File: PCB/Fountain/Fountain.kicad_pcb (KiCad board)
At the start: 2 copper layers, 100 x 86.6 mm, 29 parts, among them CN1 GROVE_IIC_5V, CN2 GROVE_IIC_5V, CN3 USB_A, CN4 AudioJack3_SwitchTR, CN5 Micro_SD_Card_Det_Hirose_DM3AT, J1 Speaker, SW1 MDOE, SW2 NEXT/VOL+, SW3 PREV/VOL-, U1 SeeeduinoXIAO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

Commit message: (Fountain) 基板位置仮決め #77
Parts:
- removed C1, C2: 100u, Capacitor_THT:CP_Radial_D6.3mm_P2.50mm
- removed CN5: Micro_SD_Card_Det_Hirose_DM3AT, Connector_Card:microSD_HC_Hirose_DM3AT-SF-PEJM5
- removed J1: Speaker, Connector_PinHeader_2.54mm:PinHeader_1x02_P2.54mm_Vertical
- removed R3, R4, R5: 4.7k, Resistor_THT:R_Axial_DIN0207_L6.3mm_D2.5mm_P7.62mm_Horizontal
- removed R6, R7: 1k, Resistor_THT:R_Axial_DIN0207_L6.3mm_D2.5mm_P7.62mm_Horizontal
- removed RV1: BRIGHTNESS, Potentiometer_THT:Potentiometer_Alps_RK097_Dual_Horizontal
- removed RV2: VOLUME, Potentiometer_THT:Potentiometer_Alps_RK097_Dual_Horizontal
- removed U1: SeeeduinoXIAO, extsui:SeeeduinoXIAO
- removed U2: DFPlayerMini, extsui:DFPlayerMini
- removed U3: OLED_128x64_IIC, extsui:OLED_128x64_0.96inch
- added BZ1: Buzzer, Buzzer_Beeper:Buzzer_TDK_PS1240P02BT_D12.2mm_H6.5mm, F.Cu at (152.5, 105.2)
- added IC1: XIAO-ESP32-C3, extsui:SeeeduinoXIAO, F.Cu at (130.0, 62.0)
- added IC2: AE-PCA9306, Package_DIP:DIP-8_W7.62mm_Socket, F.Cu at (142.5, 84.8)
- added VOL1: (TBD), Potentiometer_THT:Potentiometer_Alps_RK097_Dual_Horizontal, F.Cu at (115.5, 143.0)
- added VOL2: (TBD), Potentiometer_THT:Potentiometer_Alps_RK097_Dual_Horizontal, F.Cu at (139.5, 143.0)
- CN1: value GROVE_IIC_5V -> Conn_01x05_Female; footprint Connector:NS-Tech_Grove_1x04_P2mm_Vertical -> Connector_PinHeader_2.54mm:PinHeader_1x05_P2.54mm_Vertical
- CN2: value GROVE_IIC_5V -> CardEdgeConnector5P; footprint Connector:NS-Tech_Grove_1x04_P2mm_Vertical -> extsui:CONN_CARD_EDGE_395-010-521-201
- CN3: value USB_A -> GROVE_IIC_5V; footprint OPL_Connector:USB4+2P-2.0-90D -> OPL_Connector:HW4-2.0-90D
- CN4: value AudioJack3_SwitchTR -> GROVE_IIC_5V; footprint Connector_Audio:Jack_3.5mm_Ledino_KB3SPRS_Horizontal -> OPL_Connector:HW4-2.0-90D
- R1: value 4.7k -> 10k
- R2: value 4.7k -> 1k
- SW1: value MDOE -> (TBD)
- SW2: value NEXT/VOL+ -> (TBD)
- SW3: value PREV/VOL- -> DIPSW-4P; footprint Button_Switch_THT:SW_PUSH_6mm_H8.5mm -> Button_Switch_THT:SW_DIP_SPSTx04_Slide_9.78x12.34mm_W7.62mm_P2.54mm
- moved SW3 52.5 mm to (101.8, 108.5), turned to 90 degrees
- moved CN2 38.5 mm to (130.0, 105.0)
- moved SW1 35.5 mm to (97.8, 121.5), turned to 300 degrees
- moved CN4 30.6 mm to (161.8, 85.8), turned to 300 degrees
- moved CN1 25.0 mm to (125.2, 92.8), turned to 90 degrees
- moved R1 14.7 mm to (145.5, 77.2), turned to 90 degrees
- moved R2 14.4 mm to (145.0, 98.2), turned to 0 degrees
- moved SW2 9.04 mm to (160.5, 124.8)
- moved CN3 4.31 mm to (98.0, 85.8), turned to 60 degrees
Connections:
- CN1 pad 1: SCL -> 5V
- CN1 pad 2: SDA -> SDA_5V
- CN1 pad 3: 5V -> SCL_5V
- CN1 pad 4: GND -> Net-(CN1-Pad4)
- CN2 pad 1: SCL -> 5V
- CN2 pad 2: SDA -> SDA_5V
- CN2 pad 3: 5V -> SCL_5V
- CN2 pad 4: GND -> Net-(CN2-Pad4)
- CN3 pad 1: 5V -> SCL_5V
- CN3 pad 2: Net-(CN3-Pad2) -> SDA_5V
- CN3 pad 3: Net-(CN3-Pad3) -> 5V
- R1 pad 1: 3V3 -> Net-(IC1-Pad9)
- R1 pad 2: SDA -> 3V3
- R2 pad 1: 3V3 -> Net-(IC1-Pad7)
- R2 pad 2: SCL -> Net-(BZ1-Pad1)
- SW1 pad 1: Net-(SW1-Pad1) -> Net-(IC1-Pad9)
- SW3 pad 1: Net-(SW3-Pad1) -> GND
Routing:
- net 3V3: track 185.6 -> 0.00 mm
- net GND: track 131.3 -> 0.00 mm, vias 283 -> 58
- net 5V: track 110.0 -> 0.00 mm
- net RV_V: track 96.9 -> 0.00 mm, vias 2 -> 0
- net Net-(SW1-Pad1): track 87.7 -> 0.00 mm, vias 2 -> 0
- net MOSI: track 82.9 -> 0.00 mm
- net MISO: track 82.8 -> 0.00 mm, vias 1 -> 0
- net SCK: track 78.6 -> 0.00 mm, vias 1 -> 0
- net SCL: track 75.0 -> 0.00 mm, vias 1 -> 0
- net SDA: track 71.7 -> 0.00 mm, vias 1 -> 0
- net RV_B: track 70.2 -> 0.00 mm, vias 2 -> 0
- net Net-(IC1-Pad10): track 66.8 -> 0.00 mm
- net CS: track 60.6 -> 0.00 mm, vias 1 -> 0
- net Net-(SW3-Pad1): track 58.6 -> 0.00 mm
- net TXD: track 52.2 -> 0.00 mm, vias 1 -> 0
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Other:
- board text added: "@ext_sui 2023.10"
- board text added: "Fountain v1.0"
- board text removed: "@ext_sui 2021.09"
- board text removed: "BRIGHTNESS"
- board text removed: "C"
- board text removed: "D"
- board text removed: "G"
- board text removed: "MODE"
- board text removed: "NEXT+"
- board text removed: "PREV-"
- board text removed: "SPK"
- board text removed: "Ship Growing v1.0"
- board text removed: "V"
- board text removed: "VOLUME"

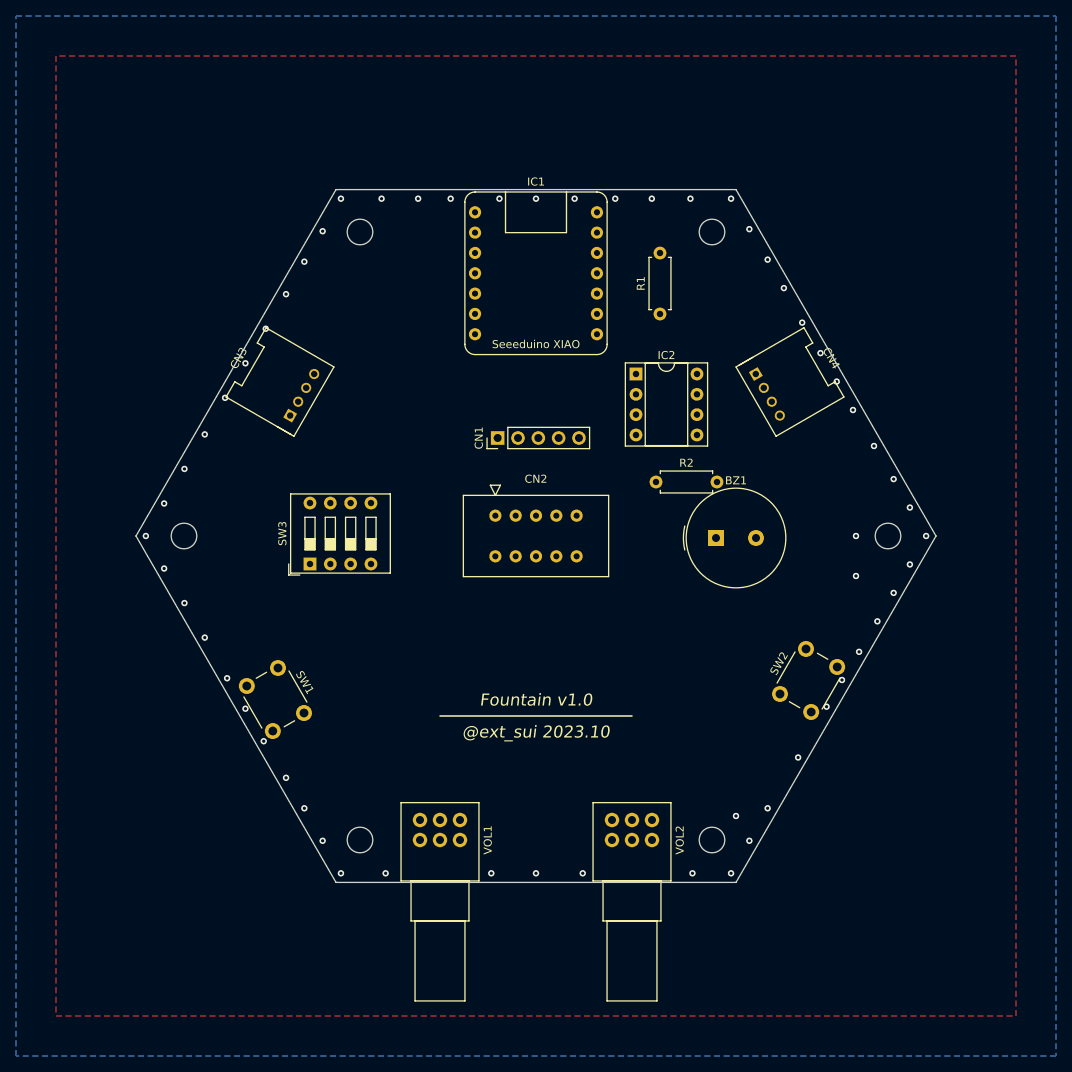
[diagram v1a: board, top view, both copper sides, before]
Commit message: (Fountain) JTAG コネクタと電解コンを追加および VOL/SW 位置調整 #77
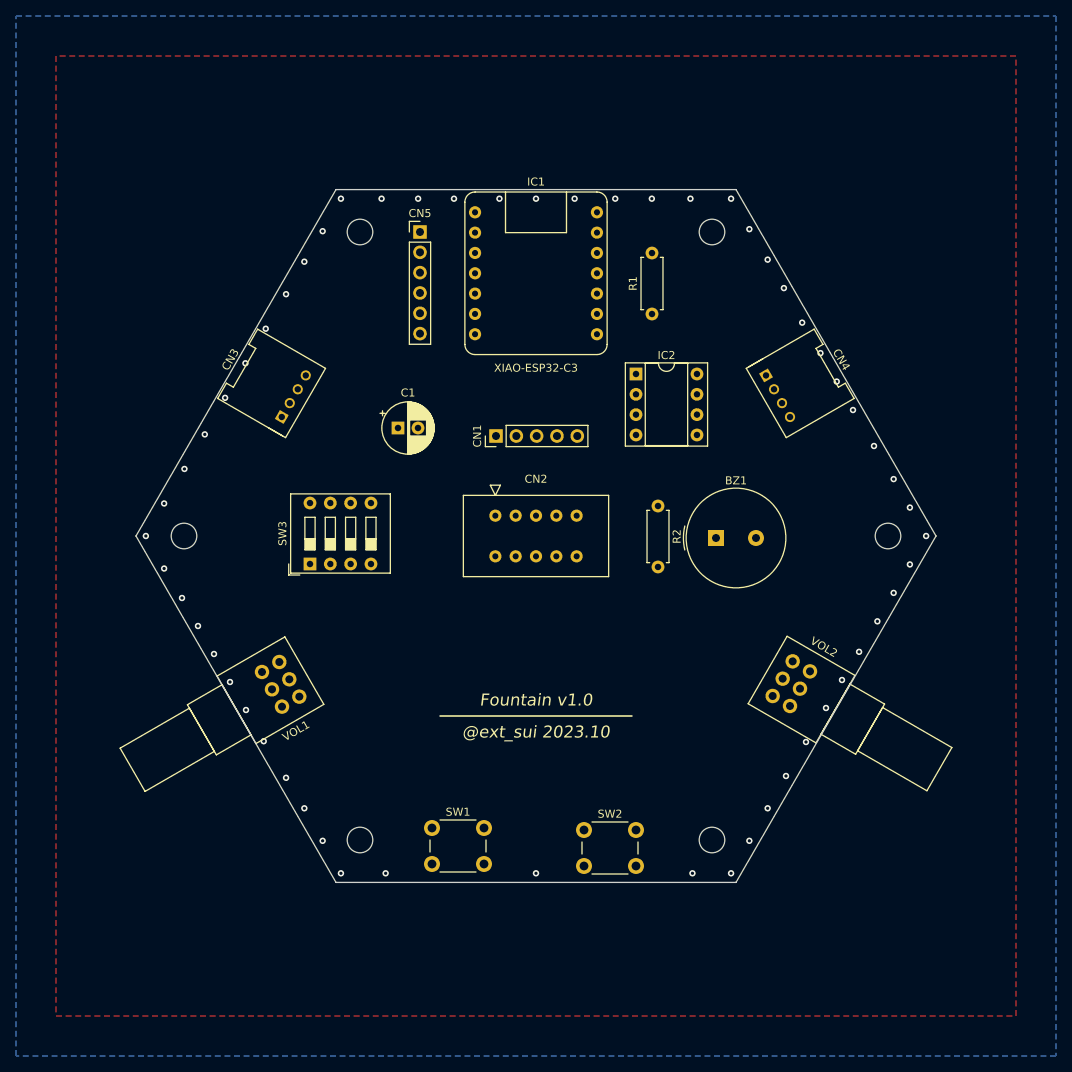
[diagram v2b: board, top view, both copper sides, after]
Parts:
- added C1: CP, Capacitor_THT:CP_Radial_D6.3mm_P2.50mm, F.Cu at (112.8, 91.5)
- added CN5: JTAG, Connector_PinHeader_2.54mm:PinHeader_1x06_P2.54mm_Vertical, F.Cu at (115.5, 67.0)
- moved SW2 29.8 mm to (136.0, 141.8), turned to 0 degrees
- moved VOL1 28.8 mm to (95.8, 122.0), turned to 210 degrees
- moved VOL2 27.9 mm to (161.8, 126.2), turned to 330 degrees
- moved SW1 27.8 mm to (117.0, 141.5), turned to 0 degrees
- moved R2 3.01 mm to (145.2, 101.2), turned to 270 degrees
- moved CN4 1.29 mm to (163.0, 85.9)
- moved CN3 1.06 mm to (97.0, 85.9)
- moved R1 1.00 mm to (144.5, 77.2)
- moved CN1 0.33 mm to (125.0, 92.5)
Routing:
- net GND: vias 58 -> 55

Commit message: (Fountain) 部品位置仮決めとシルク追加 #77
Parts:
- moved BZ1 1.00 mm to (153.5, 105.2)
- moved SW1 1.00 mm to (118.0, 141.5)
- moved SW2 0.56 mm to (135.5, 141.5)
- moved SW3 0.31 mm to (101.8, 108.8)
- moved R2 0.25 mm to (145.5, 101.2)
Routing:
- net GND: vias 55 -> 59
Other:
- board text added: "+5V"
- board text added: "GND"
- board text added: "TCK"
- board text added: "TDI"
- board text added: "TDO"
- board text added: "TMS"

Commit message: (Fountain) 配線試行 #77
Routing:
- net 5V: track 0.00 -> 154.5 mm
- net SCL_5V: track 0.00 -> 115.6 mm
- net RV2: track 0.00 -> 97.9 mm
- net SDA_5V: track 0.00 -> 94.6 mm
- net RV1: track 0.00 -> 80.2 mm
- net Net-(CN5-Pad3): track 0.00 -> 45.9 mm
- net Net-(IC1-Pad7): track 0.00 -> 42.3 mm, vias 0 -> 1
- net Net-(CN5-Pad4): track 0.00 -> 42.0 mm
- net Net-(CN5-Pad5): track 0.00 -> 38.4 mm
- net Net-(CN5-Pad6): track 0.00 -> 34.5 mm
- net SDA_3V3: track 0.00 -> 22.6 mm
- net 3V3: track 0.00 -> 22.5 mm
- net GND: track 0.00 -> 15.1 mm
- net SCL_3V3: track 0.00 -> 10.9 mm
- net Net-(BZ1-Pad1): track 0.00 -> 9.50 mm
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
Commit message: (Fountain) 配線第0版完成 #77
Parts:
- moved BZ1 3.59 mm to (156.0, 107.8), turned to 90 degrees
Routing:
- net 3V3: track 22.5 -> 136.4 mm, vias 0 -> 3
- net Net-(IC1-Pad9): track 6.88 -> 87.2 mm, vias 0 -> 1
- net Net-(IC1-Pad10): track 0.00 -> 76.9 mm, vias 0 -> 1
- net SDA_5V: track 94.6 -> 111.6 mm, vias 1 -> 0
- net GND: track 15.1 -> 0.11 mm, vias 59 -> 61
- net RV1: track 80.2 -> 84.2 mm, vias 0 -> 2
- net RV2: track 97.9 -> 94.9 mm, vias 0 -> 2
- net Net-(IC1-Pad7): track 42.3 -> 40.0 mm
- net Net-(CN5-Pad3): track 45.9 -> 47.7 mm
- net Net-(BZ1-Pad1): track 9.50 -> 11.0 mm
- net Net-(CN5-Pad4): track 42.0 -> 43.4 mm
- net SCL_5V: track 115.6 -> 114.5 mm
- net Net-(CN5-Pad5): track 38.4 -> 38.9 mm
- net Net-(VOL1-Pad1): vias 1 -> 0

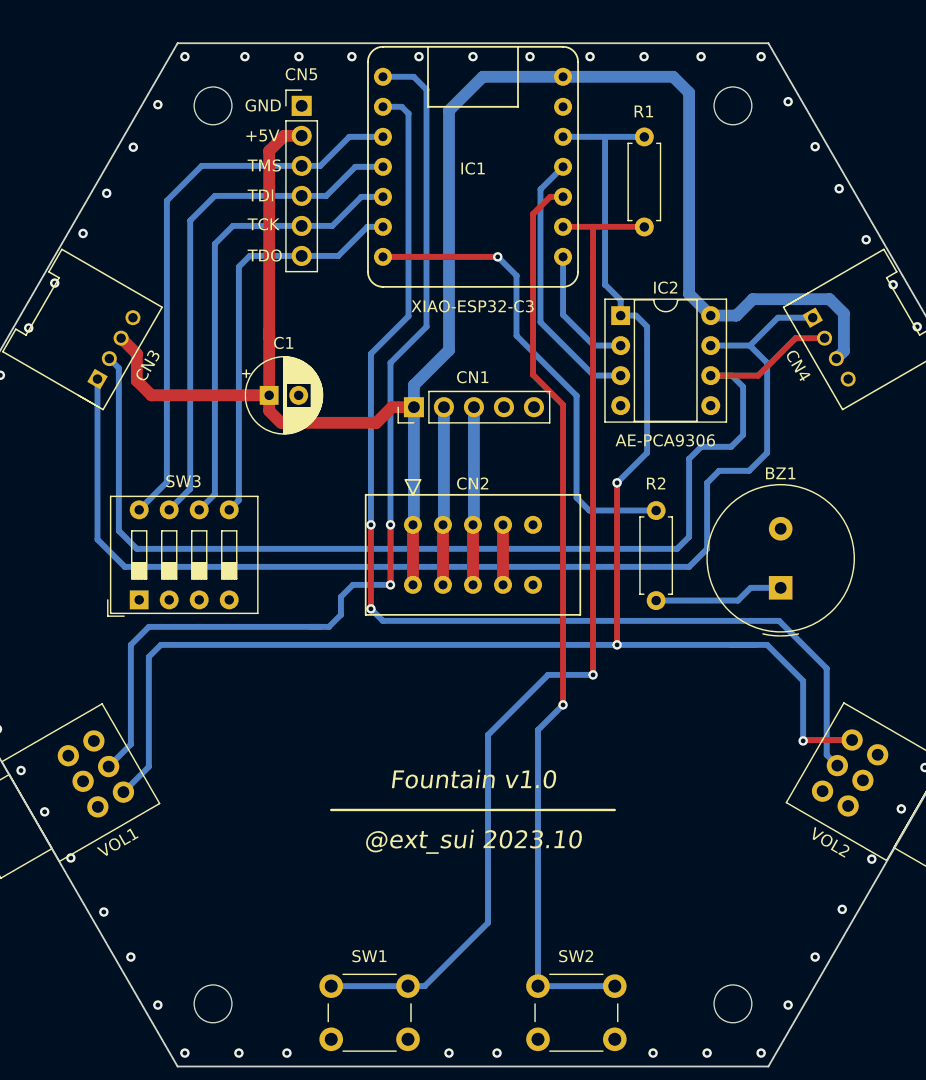
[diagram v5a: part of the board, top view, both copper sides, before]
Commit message: (Fountain) 配線調整とシルク修正 #77
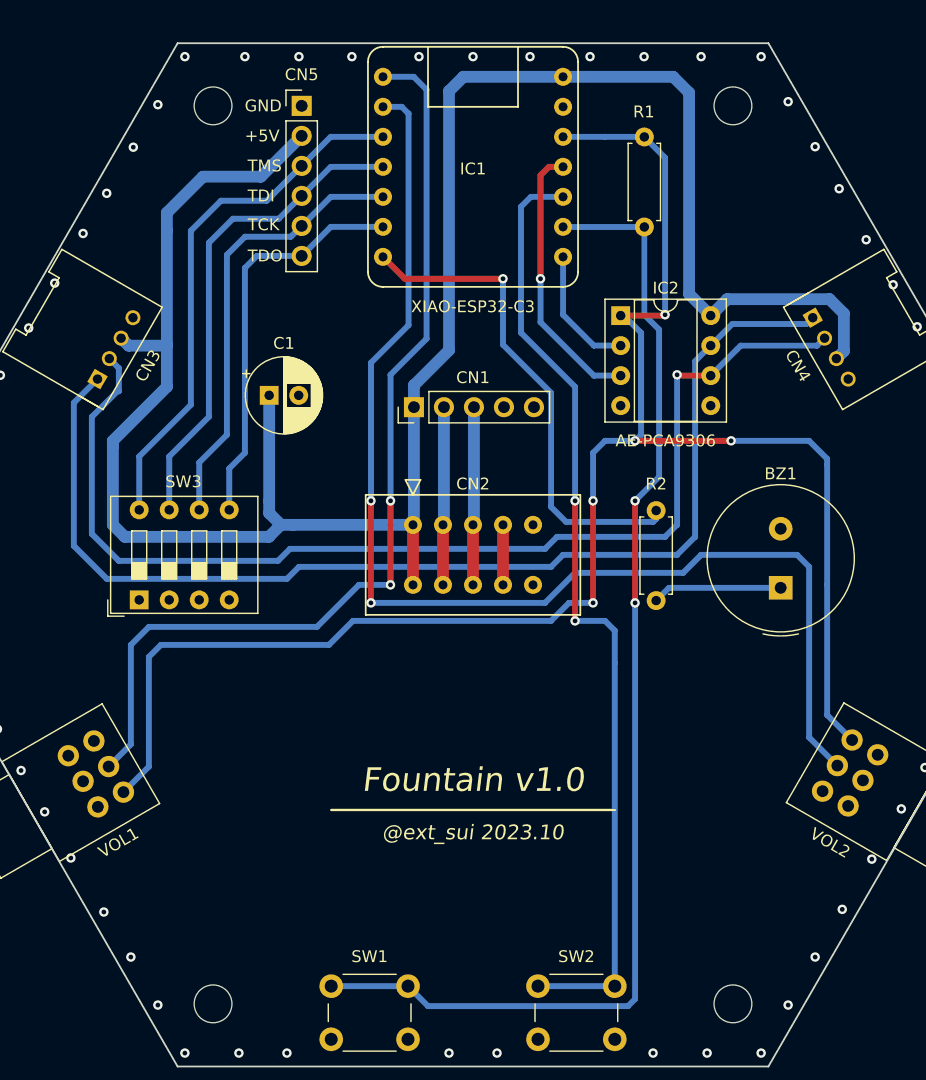
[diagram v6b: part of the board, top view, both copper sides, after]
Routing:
- net 5V: track 154.4 -> 184.7 mm
- net 3V3: track 136.4 -> 155.8 mm, vias 3 -> 5
- net Net-(IC1-Pad9): track 87.2 -> 100.3 mm, vias 1 -> 2
- net RV2: track 94.9 -> 102.1 mm
- net Net-(IC1-Pad10): track 76.9 -> 81.1 mm, vias 1 -> 2
- net Net-(CN5-Pad3): track 47.7 -> 45.0 mm
- net Net-(IC1-Pad7): track 40.0 -> 42.1 mm
- net Net-(CN5-Pad4): track 43.4 -> 41.4 mm
- net RV1: track 84.2 -> 82.6 mm
- net SCL_5V: track 114.5 -> 113.2 mm
- net Net-(CN5-Pad5): track 38.9 -> 37.8 mm
- net SDA_3V3: track 22.6 -> 23.3 mm, vias 0 -> 1
- net SDA_5V: track 111.6 -> 111.7 mm, vias 0 -> 1

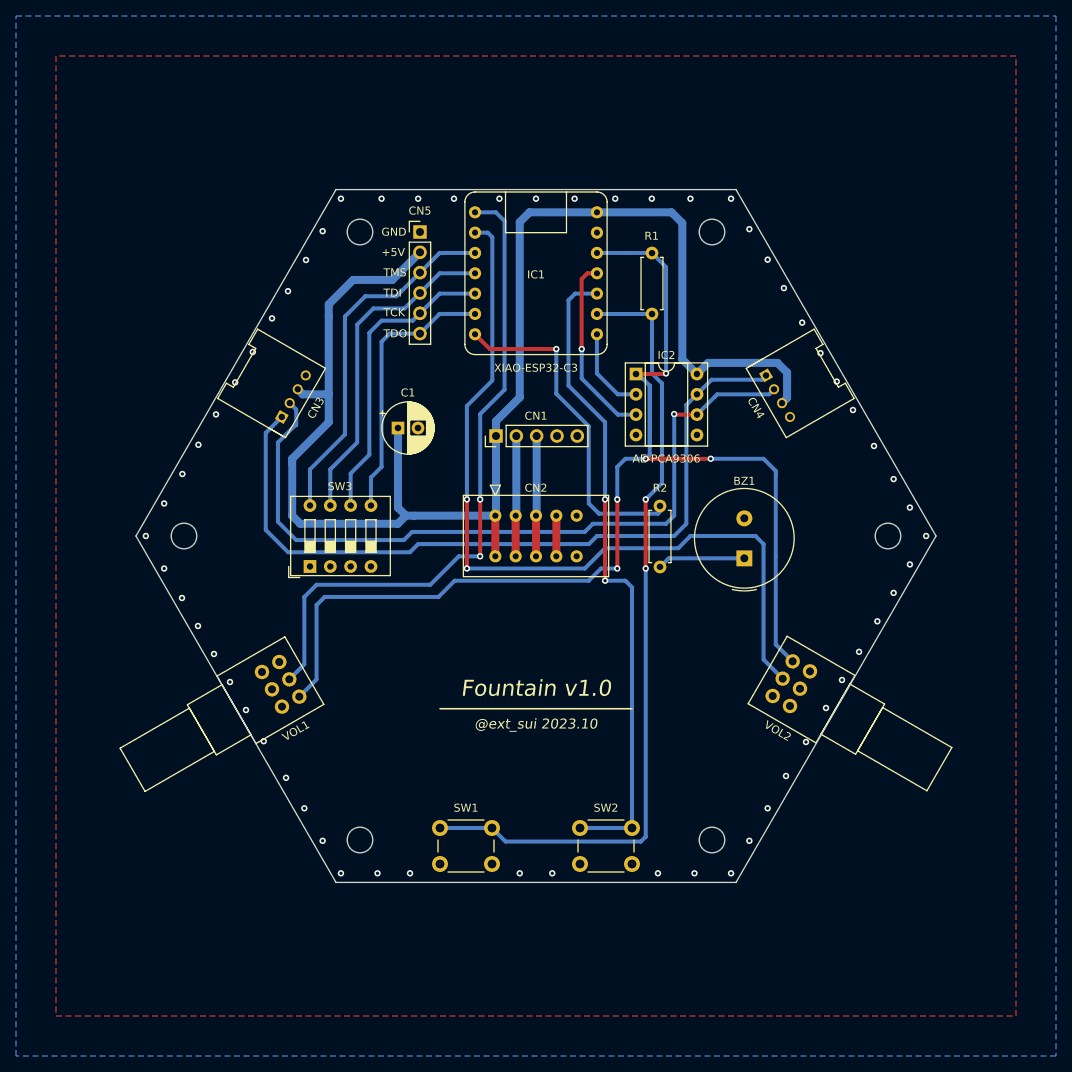
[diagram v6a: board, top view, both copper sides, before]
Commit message: (Fountain) GND ビア打ちとティアドロップ追加 #77
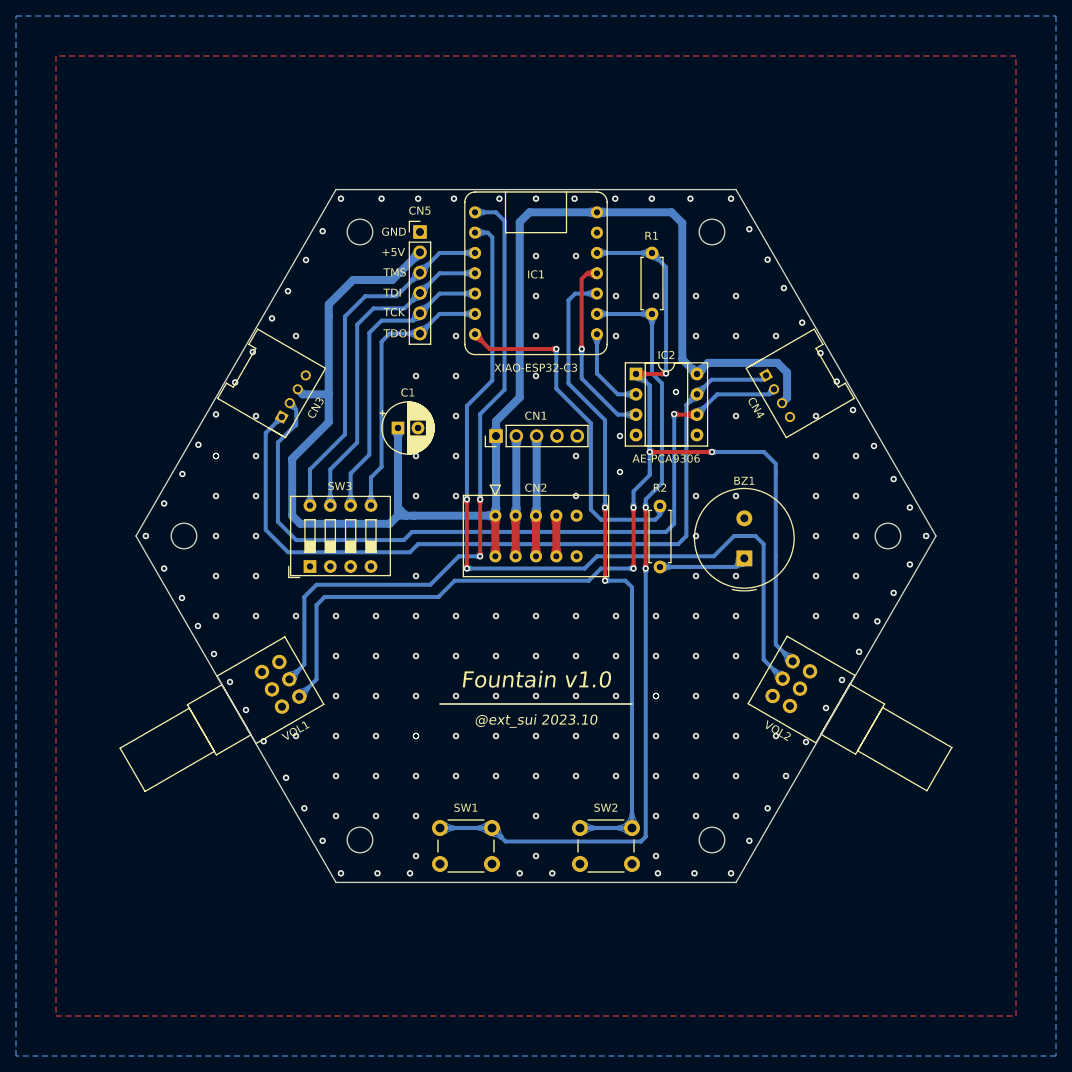
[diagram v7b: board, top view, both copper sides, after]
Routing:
- net 5V: track 184.7 -> 195.7 mm
- net 3V3: track 155.8 -> 164.9 mm
- net Net-(IC1-Pad7): track 42.1 -> 43.3 mm
- net SCL_5V: track 113.2 -> 114.1 mm
- net SDA_5V: track 111.7 -> 112.3 mm
- net GND: vias 61 -> 188
